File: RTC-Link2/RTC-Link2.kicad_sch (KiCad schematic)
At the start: 20 parts, among them CN1 EDGE_CON_02x12, J1 LinkHeader, J2 Flyout1, J3 Flyout2, P1 c64cartedge, U1 MC68A21, U2 74LS30, U3 74LS00, U4 2764

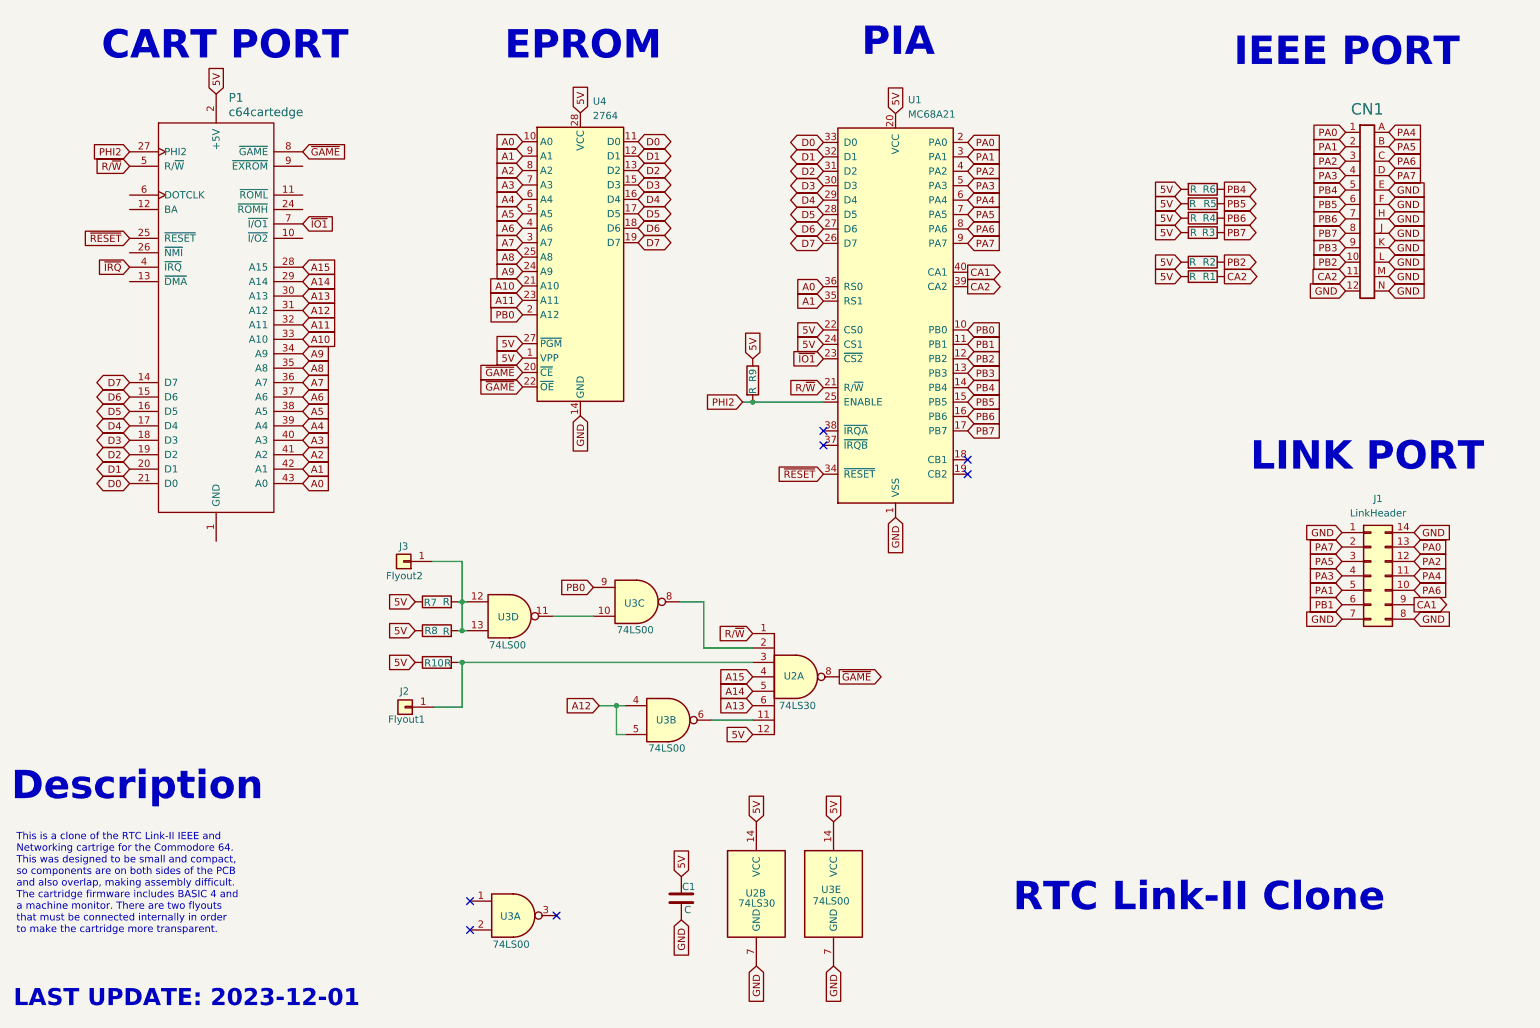
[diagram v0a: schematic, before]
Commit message: Update original to V1.1. R9 fix.
I populated the V1.0 "plus" version pcb and discovered an error with R9. It was manually corrected on the pcb and the design works correctly. This original board requires the same fix.

This V1.1 update **should** work but has not been tested as of yet. Use at own risk!

 Added component values on schematic. Updated files to work on Kicad 9. Added readme file.
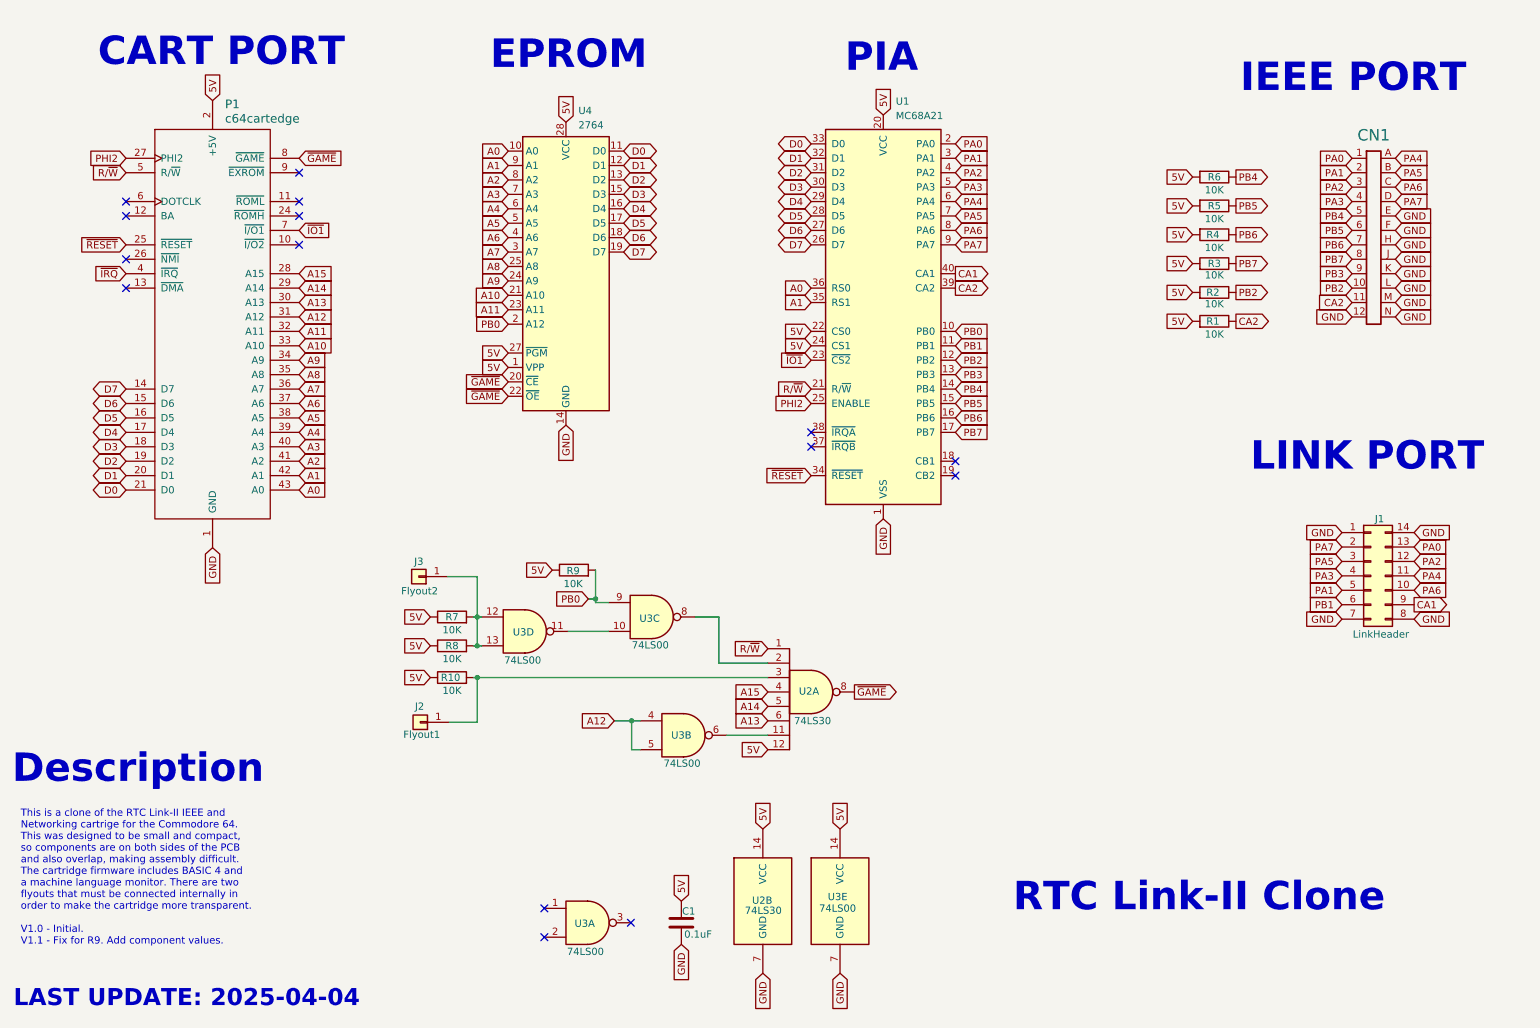
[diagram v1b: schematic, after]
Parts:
- C1: value C -> 0.1uF
- R1, R10, R2, R3, R4, R5, R6, R7, R8, R9: value R -> 10K
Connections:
- net PB0: now also R9.2
- net PHI2: no longer R9.2
- no-connect marks 7 -> 15
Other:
- note added: "LAST UPDATE: 2025-04-04"
- note added: "This is a clone of the RTC Link-II IEEE and Networking cartrige for the Commodore 64. This was designed to be small and compact, so components are on both sides of the PCB and also overlap, making assembly difficult. The cartridge firmware includes BASIC 4 and a machine language monitor. There are two flyouts that must be connected internally in order to make the cartridge more transparent. V1.0 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"
- note removed: "LAST UPDATE: 2023-12-01"
- note removed: "This is a clone of the RTC Link-II IEEE and Networking cartrige for the Commodore 64. This was designed to be small and compact, so components are on both sides of the PCB and also overlap, making assembly difficult. The cartridge firmware includes BASIC 4 and a machine monitor. There are two flyouts that must be connected internally in order to make the cartridge more transparent."
- company: (none) -> Steve J. Gray
- title: (none) -> RTC-Link II Clone
- moved on the sheet: C1, CN1, J2, J3, P1, R1, R10, R2, R3, R4, R5, R6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
